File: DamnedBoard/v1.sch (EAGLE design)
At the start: 21 parts, among them J1 CORTEX_DEBUG_SMD, J2 I_TEST, J3 TEST, U1 EFM32ZG108, U2 MAX44009EDT+T21-0490D-M

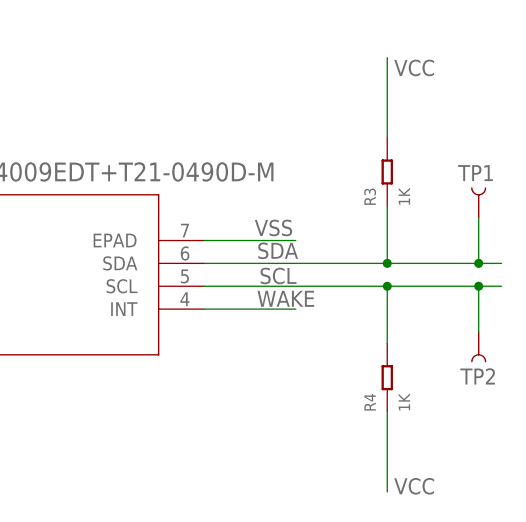
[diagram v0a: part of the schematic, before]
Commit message: Working EM4 version of the firmware.
Also increased pullups to 1.8K for lower power.
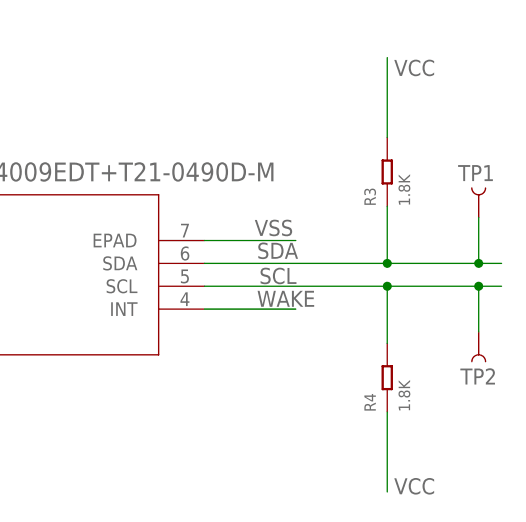
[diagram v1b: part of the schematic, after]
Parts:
- R3, R4: value 1K -> 1.8K
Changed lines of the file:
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@@
 <part name="U$1" library="boneyard" deviceset="COPYRIGHT" device=""/>
 <part name="J1" library="SparkFun-Connectors" library_urn="urn:adsk.eagle:library:513" deviceset="CORTEX_DEBUG" device="_SMD" package3d_urn="urn:adsk.eagle:package:38289/1"/>
-<part name="R3" library="Seeed-Resistor" library_urn="urn:adsk.eagle:library:474" deviceset="SMD-RES-1K-5%-1/16W(0402)" device="" package3d_urn="urn:adsk.eagle:package:32792/1" value="1K"/>
-<part name="R4" library="Seeed-Resistor" library_urn="urn:adsk.eagle:library:474" deviceset="SMD-RES-1K-5%-1/16W(0402)" device="" package3d_urn="urn:adsk.eagle:package:32792/1" value="1K"/>
+<part name="R3" library="Seeed-Resistor" library_urn="urn:adsk.eagle:library:474" deviceset="SMD-RES-1K-5%-1/16W(0402)" device="" package3d_urn="urn:adsk.eagle:package:32792/1" value="1.8K"/>
+<part name="R4" library="Seeed-Resistor" library_urn="urn:adsk.eagle:library:474" deviceset="SMD-RES-1K-5%-1/16W(0402)" device="" package3d_urn="urn:adsk.eagle:package:32792/1" value="1.8K"/>
 <part name="TP1" library="SparkFun-Connectors" library_urn="urn:adsk.eagle:library:513" deviceset="TEST-POINT" device="3X5" package3d_urn="urn:adsk.eagle:package:38285/1"/>
 <part name="TP2" library="SparkFun-Connectors" library_urn="urn:adsk.eagle:library:513" deviceset="TEST-POINT" device="3X5" package3d_urn="urn:adsk.eagle:package:38285/1"/>

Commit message: Moving to ADC for trimmer.
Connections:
- net ADJ: now also U1.PD6; no longer U1.PC1
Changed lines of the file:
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@@
 <?xml version="1.0" encoding="utf-8"?>
 <!DOCTYPE eagle SYSTEM "eagle.dtd">
-<eagle version="8.3.1">
+<eagle version="8.3.2">
 <drawing>
 <settings>
@@
 <net name="ADJ" class="0">
 <segment>
-<pinref part="U1" gate="G$1" pin="PC1"/>
-<wire x1="43.18" y1="71.12" x2="30.48" y2="71.12" width="0.1524" layer="91"/>
-<label x="30.988" y="71.374" size="1.778" layer="95"/>
-</segment>
-<segment>
 <pinref part="R5" gate="A" pin="2"/>
 <wire x1="-66.04" y1="71.12" x2="-66.04" y2="78.74" width="0.1524" layer="91"/>
 <label x="-64.516" y="76.708" size="1.778" layer="95"/>
 </segment>
-</net>
+<segment>
+<pinref part="U1" gate="G$1" pin="PD6"/>
+<wire x1="111.76" y1="78.74" x2="124.46" y2="78.74" width="0.1524" layer="91"/>
+<label x="119.634" y="79.248" size="1.778" layer="95"/>
+</segment>
+</net>

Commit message: V1.1 locked. Ordered from OSH park.
All perphierals working in the firmware. Just need to finish some features and tune.
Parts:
- removed J3: TEST, SparkFun-Connectors:CONN_02
- removed JP2: JUMPER-SMT_2_NC_TRACE_NO-SILK, SparkFun-Jumpers:JUMPER-SMT_2_NC_TRACE_NO-SILK
- J2: value I_TEST -> GND
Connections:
- removed net +L: G1.+$1, JP2.2
- removed net +R: G1.+$2, J3.2
- net VCC: now also G1.+$1, G1.+$2; no longer J2.1, JP2.1
- net VSS: now also J2.1; no longer J3.1
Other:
- moved on the sheet: J2
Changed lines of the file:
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@@
 <part name="C6" library="SparkFun-Capacitors" library_urn="urn:adsk.eagle:library:510" deviceset="10UF" device="-0805-10V-10%" package3d_urn="urn:adsk.eagle:package:37429/1" value="10uF"/>
 <part name="G1" library="boneyard" deviceset="LINX_BAT_HLD_001" device="" package3d_urn="urn:adsk.eagle:package:291704/2"/>
-<part name="JP2" library="SparkFun-Jumpers" library_urn="urn:adsk.eagle:library:528" deviceset="JUMPER-SMT_2_NC_TRACE" device="_NO-SILK" package3d_urn="urn:adsk.eagle:package:39286/1"/>
 <part name="U$1" library="boneyard" deviceset="COPYRIGHT" device=""/>
 <part name="J1" library="SparkFun-Connectors" library_urn="urn:adsk.eagle:library:513" deviceset="CORTEX_DEBUG" device="_SMD" package3d_urn="urn:adsk.eagle:package:38289/1"/>
@@
 <part name="TP1" library="SparkFun-Connectors" library_urn="urn:adsk.eagle:library:513" deviceset="TEST-POINT" device="3X5" package3d_urn="urn:adsk.eagle:package:38285/1"/>
 <part name="TP2" library="SparkFun-Connectors" library_urn="urn:adsk.eagle:library:513" deviceset="TEST-POINT" device="3X5" package3d_urn="urn:adsk.eagle:package:38285/1"/>
-<part name="J2" library="SparkFun-Connectors" library_urn="urn:adsk.eagle:library:513" deviceset="CONN_01" device="" package3d_urn="urn:adsk.eagle:package:38028/1" value="I_TEST"/>
-<part name="J3" library="SparkFun-Connectors" library_urn="urn:adsk.eagle:library:513" deviceset="CONN_02" device="" package3d_urn="urn:adsk.eagle:package:38039/1" value="TEST"/>
 <part name="R5" library="boneyard" deviceset="23BR100KLFTR" device=""/>
 <part name="C3" library="Seeed-Capacitor" library_urn="urn:adsk.eagle:library:464" deviceset="CERAMIC-10NF-50V-10%-X7R(0402)" device="" package3d_urn="urn:adsk.eagle:package:32379/1" value="10nf"/>
@@
 <part name="VSS3" library="SparkFun-PowerSymbols" library_urn="urn:adsk.eagle:library:530" deviceset="GND2" device="" value="VSS"/>
 <part name="VSS4" library="SparkFun-PowerSymbols" library_urn="urn:adsk.eagle:library:530" deviceset="GND2" device="" value="VSS"/>
+<part name="J2" library="SparkFun-Connectors" library_urn="urn:adsk.eagle:library:513" deviceset="CONN_01" device="" package3d_urn="urn:adsk.eagle:package:38028/1" value="GND"/>
 </parts>
 <sheets>
@@
 <instance part="C6" gate="G$1" x="5.08" y="71.12"/>
 <instance part="G1" gate="G$1" x="50.8" y="12.7"/>
-<instance part="JP2" gate="G$1" x="35.56" y="15.24" smashed="yes">
-<attribute name="NAME" x="33.02" y="17.78" size="1.778" layer="95" font="vector"/>
-</instance>
 <instance part="U$1" gate="G$1" x="48.26" y="101.6"/>
 <instance part="J1" gate="G$1" x="-25.4" y="33.02"/>
@@
 <attribute name="NAME" x="168.148" y="6.858" size="1.778" layer="95" font="vector"/>
 </instance>
-<instance part="J2" gate="G$1" x="-5.08" y="101.6"/>
-<instance part="J3" gate="G$1" x="-5.08" y="116.84"/>
 <instance part="R5" gate="A" x="-76.2" y="63.5" smashed="yes">
 <attribute name="NAME" x="-75.8444" y="58.5724" size="1.778" layer="95" ratio="10" rot="SR0"/>
@@
 <instance part="VSS3" gate="G$1" x="142.24" y="56.642"/>
 <instance part="VSS4" gate="G$1" x="129.54" y="95.758" rot="R180"/>
+<instance part="J2" gate="G$1" x="0" y="116.84"/>
 </instances>
 <busses>
@@
 </segment>
 <segment>
-<pinref part="J3" gate="G$1" pin="1"/>
-<wire x1="2.54" y1="116.84" x2="10.16" y2="116.84" width="0.1524" layer="91"/>
-<label x="5.588" y="117.094" size="1.778" layer="95"/>
-</segment>
-<segment>
 <pinref part="C3" gate="G$1" pin="1"/>
 <pinref part="VSS" gate="G$1" pin="3.3V"/>
@@
 <wire x1="129.54" y1="88.9" x2="129.54" y2="93.218" width="0.1524" layer="91"/>
 </segment>
+<segment>
+<pinref part="J2" gate="G$1" pin="1"/>
+<wire x1="7.62" y1="116.84" x2="17.78" y2="116.84" width="0.1524" layer="91"/>
+<label x="12.954" y="117.602" size="1.778" layer="95"/>
+</segment>
 </net>
 <net name="SDA" class="0">
@@
 </segment>
 </net>
-<net name="+R" class="0">
-<segment>
-<pinref part="G1" gate="G$1" pin="+$2"/>
-<wire x1="48.26" y1="10.16" x2="40.64" y2="10.16" width="0.1524" layer="91"/>
-<label x="41.402" y="10.414" size="1.778" layer="95"/>
-</segment>
-<segment>
-<pinref part="J3" gate="G$1" pin="2"/>
-<wire x1="2.54" y1="119.38" x2="10.16" y2="119.38" width="0.1524" layer="91"/>
-<label x="5.842" y="119.888" size="1.778" layer="95"/>
-</segment>
-</net>
-<net name="+L" class="0">
-<segment>
-<pinref part="G1" gate="G$1" pin="+$1"/>
-<pinref part="JP2" gate="G$1" pin="2"/>
-<wire x1="48.26" y1="15.24" x2="40.64" y2="15.24" width="0.1524" layer="91"/>
-<label x="41.656" y="16.002" size="1.778" layer="95"/>
-</segment>
-</net>
 <net name="SWDCLK" class="0">
 <segment>
@@
 <wire x1="-40.64" y1="38.1" x2="-50.8" y2="38.1" width="0.1524" layer="91"/>
 <label x="-50.546" y="38.608" size="1.778" layer="95"/>
-</segment>
-<segment>
-<pinref part="JP2" gate="G$1" pin="1"/>
-<wire x1="30.48" y1="15.24" x2="22.86" y2="15.24" width="0.1524" layer="91"/>
-<label x="22.86" y="15.748" size="1.778" layer="95"/>
 </segment>
 <segment>
@@
 <wire x1="88.9" y1="17.78" x2="78.74" y2="17.78" width="0.1524" layer="91"/>
 <label x="78.994" y="18.034" size="1.778" layer="95"/>
-</segment>
-<segment>
-<pinref part="J2" gate="G$1" pin="1"/>
-<wire x1="2.54" y1="101.6" x2="10.16" y2="101.6" width="0.1524" layer="91"/>
-<label x="4.572" y="102.362" size="1.778" layer="95"/>
 </segment>
 <segment>
@@
 <junction x="30.48" y="58.42"/>
 </segment>
-</net>
+<segment>
+<pinref part="G1" gate="G$1" pin="+$1"/>
+<wire x1="48.26" y1="15.24" x2="33.02" y2="15.24" width="0.1524" layer="91"/>
+<wire x1="33.02" y1="15.24" x2="33.02" y2="12.7" width="0.1524" layer="91"/>
+<pinref part="G1" gate="G$1" pin="+$2"/>
+<wire x1="33.02" y1="12.7" x2="33.02" y2="10.16" width="0.1524" layer="91"/>
+<wire x1="33.02" y1="10.16" x2="48.26" y2="10.16" width="0.1524" layer="91"/>
+<wire x1="33.02" y1="12.7" x2="25.4" y2="12.7" width="0.1524" layer="91"/>
+<junction x="33.02" y="12.7"/>
+<label x="25.146" y="13.208" size="1.778" layer="95"/>
+</segment>
+</net>

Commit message: Adding scheatic png
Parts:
- removed TP1, TP2: TEST-POINT3X5, SparkFun-Connectors:TEST-POINT3X5
- J2: value GND -> debug; device SparkFun-Connectors:CONN_01 -> SparkFun-Connectors:CONN_03
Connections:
- net SCL: now also J2.1; no longer TP2.1
- net SDA: now also J2.2; no longer TP1.1
- net VSS: now also J2.3; no longer J2.1
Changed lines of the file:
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@@
 <part name="R3" library="Seeed-Resistor" library_urn="urn:adsk.eagle:library:474" deviceset="SMD-RES-1K-5%-1/16W(0402)" device="" package3d_urn="urn:adsk.eagle:package:32792/1" value="1.8K"/>
 <part name="R4" library="Seeed-Resistor" library_urn="urn:adsk.eagle:library:474" deviceset="SMD-RES-1K-5%-1/16W(0402)" device="" package3d_urn="urn:adsk.eagle:package:32792/1" value="1.8K"/>
-<part name="TP1" library="SparkFun-Connectors" library_urn="urn:adsk.eagle:library:513" deviceset="TEST-POINT" device="3X5" package3d_urn="urn:adsk.eagle:package:38285/1"/>
-<part name="TP2" library="SparkFun-Connectors" library_urn="urn:adsk.eagle:library:513" deviceset="TEST-POINT" device="3X5" package3d_urn="urn:adsk.eagle:package:38285/1"/>
 <part name="R5" library="boneyard" deviceset="23BR100KLFTR" device=""/>
 <part name="C3" library="Seeed-Capacitor" library_urn="urn:adsk.eagle:library:464" deviceset="CERAMIC-10NF-50V-10%-X7R(0402)" device="" package3d_urn="urn:adsk.eagle:package:32379/1" value="10nf"/>
@@
 <part name="VSS3" library="SparkFun-PowerSymbols" library_urn="urn:adsk.eagle:library:530" deviceset="GND2" device="" value="VSS"/>
 <part name="VSS4" library="SparkFun-PowerSymbols" library_urn="urn:adsk.eagle:library:530" deviceset="GND2" device="" value="VSS"/>
-<part name="J2" library="SparkFun-Connectors" library_urn="urn:adsk.eagle:library:513" deviceset="CONN_01" device="" package3d_urn="urn:adsk.eagle:package:38028/1" value="GND"/>
+<part name="J2" library="SparkFun-Connectors" library_urn="urn:adsk.eagle:library:513" deviceset="CONN_03" device="" package3d_urn="urn:adsk.eagle:package:38063/1" value="debug"/>
 </parts>
 <sheets>
@@
 <instance part="R3" gate="G$1" x="160.02" y="30.48" rot="R90"/>
 <instance part="R4" gate="G$1" x="160.02" y="7.62" rot="R90"/>
-<instance part="TP1" gate="G$1" x="170.18" y="25.4" smashed="yes" rot="R90">
-<attribute name="NAME" x="171.958" y="31.242" size="1.778" layer="95" font="vector" rot="R180"/>
-</instance>
-<instance part="TP2" gate="G$1" x="170.18" y="12.7" smashed="yes" rot="R270">
-<attribute name="NAME" x="168.148" y="6.858" size="1.778" layer="95" font="vector"/>
-</instance>
 <instance part="R5" gate="A" x="-76.2" y="63.5" smashed="yes">
 <attribute name="NAME" x="-75.8444" y="58.5724" size="1.778" layer="95" ratio="10" rot="SR0"/>
@@
 <instance part="VSS3" gate="G$1" x="142.24" y="56.642"/>
 <instance part="VSS4" gate="G$1" x="129.54" y="95.758" rot="R180"/>
-<instance part="J2" gate="G$1" x="0" y="116.84"/>
+<instance part="J2" gate="J$1" x="5.08" y="104.14"/>
 </instances>
 <busses>
@@
 </segment>
 <segment>
-<pinref part="J2" gate="G$1" pin="1"/>
-<wire x1="7.62" y1="116.84" x2="17.78" y2="116.84" width="0.1524" layer="91"/>
-<label x="12.954" y="117.602" size="1.778" layer="95"/>
+<pinref part="J2" gate="J$1" pin="3"/>
+<wire x1="12.7" y1="106.68" x2="22.86" y2="106.68" width="0.1524" layer="91"/>
+<label x="18.796" y="107.188" size="1.778" layer="95"/>
 </segment>
 </net>
@@
 <wire x1="139.7" y1="20.32" x2="160.02" y2="20.32" width="0.1524" layer="91"/>
 <pinref part="R3" gate="G$1" pin="1"/>
-<wire x1="160.02" y1="20.32" x2="170.18" y2="20.32" width="0.1524" layer="91"/>
-<wire x1="170.18" y1="20.32" x2="172.72" y2="20.32" width="0.1524" layer="91"/>
+<wire x1="160.02" y1="20.32" x2="172.72" y2="20.32" width="0.1524" layer="91"/>
 <wire x1="160.02" y1="26.67" x2="160.02" y2="20.32" width="0.1524" layer="91"/>
 <junction x="160.02" y="20.32"/>
-<pinref part="TP1" gate="G$1" pin="1"/>
-<wire x1="170.18" y1="25.4" x2="170.18" y2="20.32" width="0.1524" layer="91"/>
-<junction x="170.18" y="20.32"/>
+</segment>
+<segment>
+<pinref part="J2" gate="J$1" pin="2"/>
+<wire x1="12.7" y1="104.14" x2="22.86" y2="104.14" width="0.1524" layer="91"/>
+<label x="18.796" y="104.394" size="1.778" layer="95"/>
 </segment>
 </net>
@@
 <wire x1="139.7" y1="17.78" x2="160.02" y2="17.78" width="0.1524" layer="91"/>
 <pinref part="R4" gate="G$1" pin="2"/>
-<wire x1="160.02" y1="17.78" x2="170.18" y2="17.78" width="0.1524" layer="91"/>
-<wire x1="170.18" y1="17.78" x2="172.72" y2="17.78" width="0.1524" layer="91"/>
+<wire x1="160.02" y1="17.78" x2="172.72" y2="17.78" width="0.1524" layer="91"/>
 <wire x1="160.02" y1="11.43" x2="160.02" y2="17.78" width="0.1524" layer="91"/>
 <junction x="160.02" y="17.78"/>
-<pinref part="TP2" gate="G$1" pin="1"/>
-<wire x1="170.18" y1="12.7" x2="170.18" y2="17.78" width="0.1524" layer="91"/>
-<junction x="170.18" y="17.78"/>
+</segment>
+<segment>
+<pinref part="J2" gate="J$1" pin="1"/>
+<wire x1="12.7" y1="101.6" x2="22.86" y2="101.6" width="0.1524" layer="91"/>
+<label x="18.796" y="101.854" size="1.778" layer="95"/>
 </segment>
 </net>
